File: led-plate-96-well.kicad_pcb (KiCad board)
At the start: 2 copper layers, 154.9 x 93.3 mm, 10 parts, among them J2 RAPC722X, U1 R-78E5.0-0.5, U2 A000053

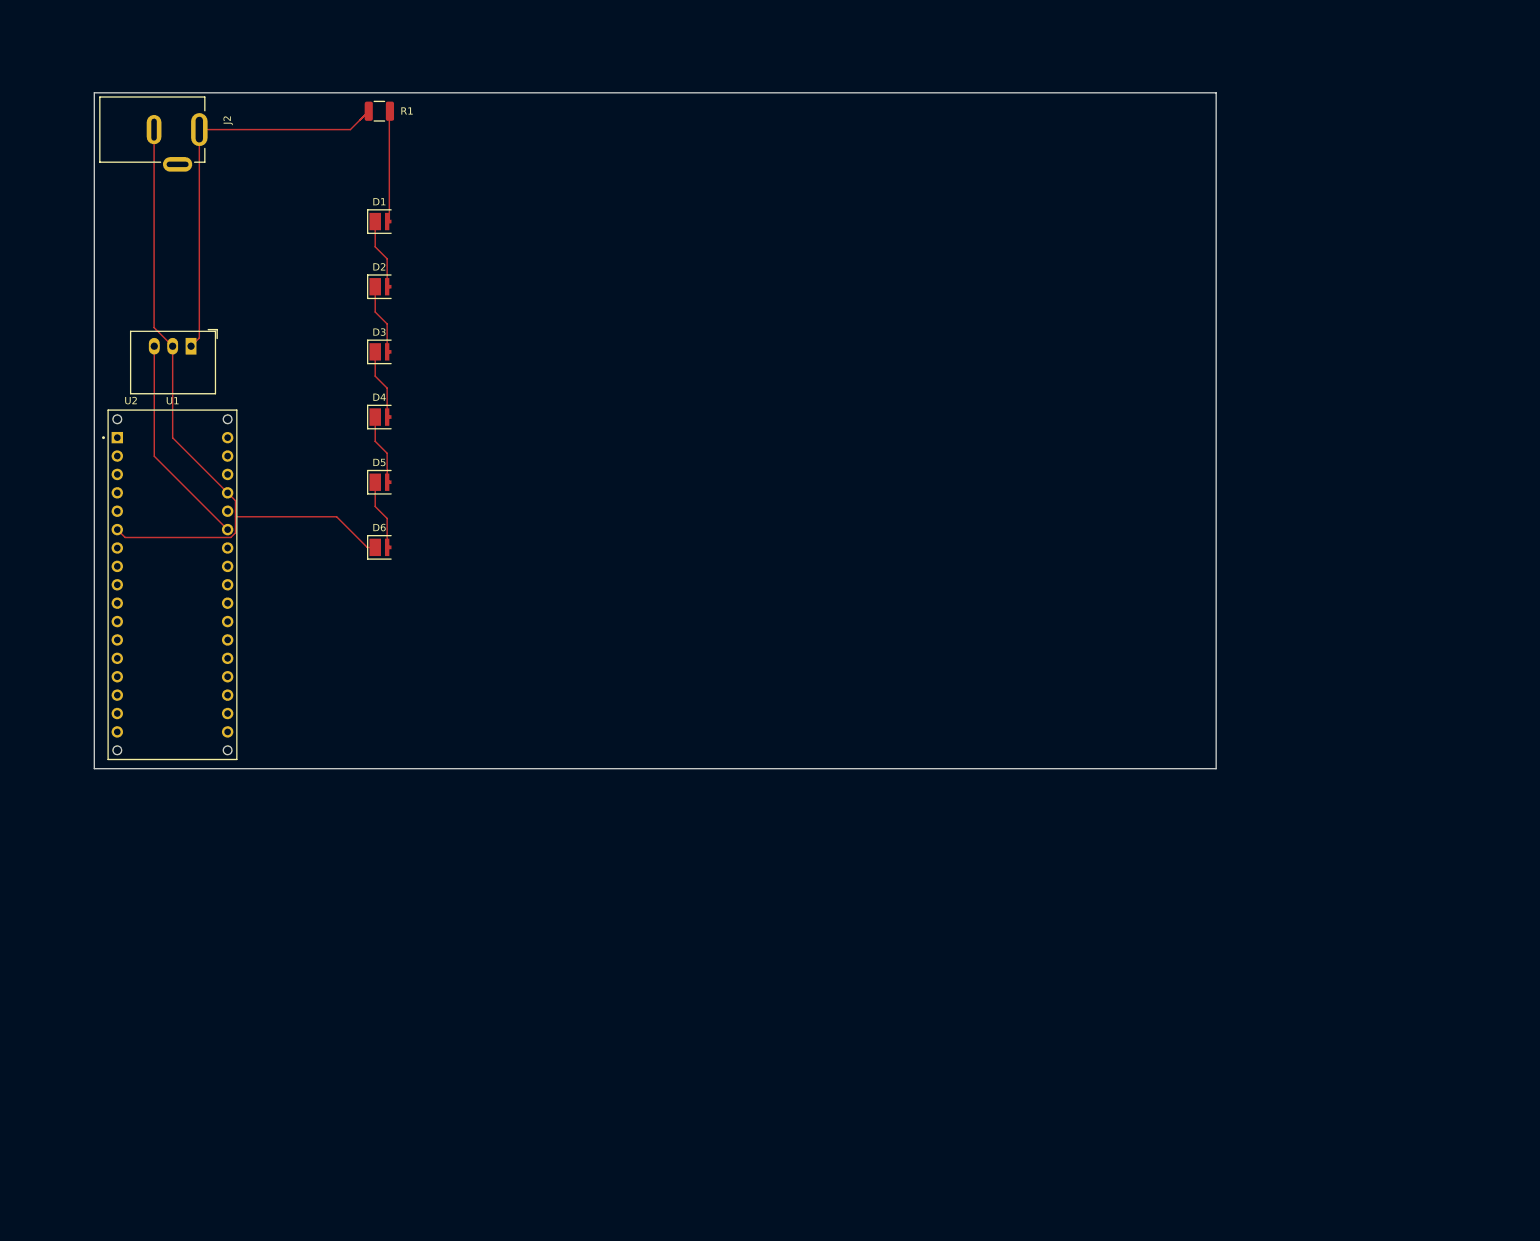
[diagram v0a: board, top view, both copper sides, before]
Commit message: basic led layout started
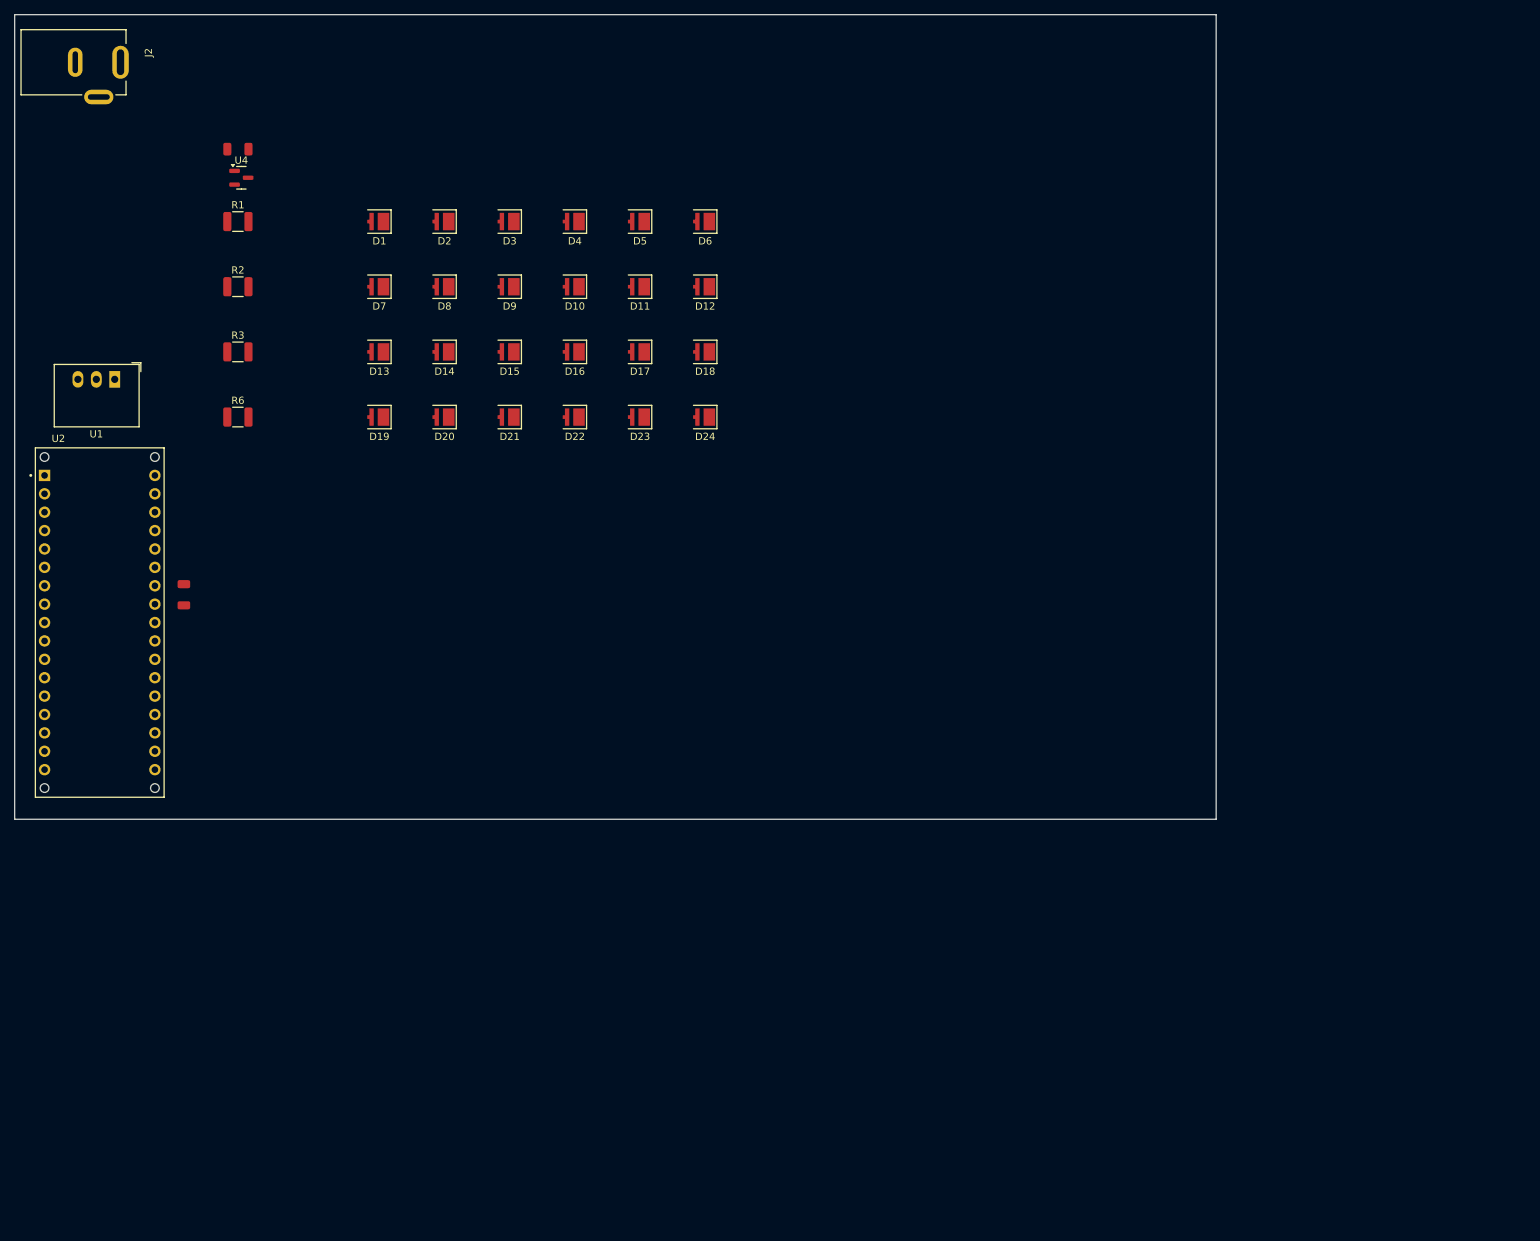
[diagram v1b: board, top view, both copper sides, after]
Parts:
- added D10: LED, LED_SMD:LED_Luminus_MP-3030-1100_3.0x3.0mm, F.Cu at (152.6, 51.2)
- added D11: LED, LED_SMD:LED_Luminus_MP-3030-1100_3.0x3.0mm, F.Cu at (161.6, 51.2)
- added D12: LED, LED_SMD:LED_Luminus_MP-3030-1100_3.0x3.0mm, F.Cu at (170.6, 51.2)
- added D13: LED, LED_SMD:LED_Luminus_MP-3030-1100_3.0x3.0mm, F.Cu at (125.6, 60.2)
- added D14: LED, LED_SMD:LED_Luminus_MP-3030-1100_3.0x3.0mm, F.Cu at (134.6, 60.2)
- added D15: LED, LED_SMD:LED_Luminus_MP-3030-1100_3.0x3.0mm, F.Cu at (143.6, 60.2)
- added D16: LED, LED_SMD:LED_Luminus_MP-3030-1100_3.0x3.0mm, F.Cu at (152.6, 60.2)
- added D17: LED, LED_SMD:LED_Luminus_MP-3030-1100_3.0x3.0mm, F.Cu at (161.6, 60.2)
- added D18: LED, LED_SMD:LED_Luminus_MP-3030-1100_3.0x3.0mm, F.Cu at (170.6, 60.2)
- added D19: LED, LED_SMD:LED_Luminus_MP-3030-1100_3.0x3.0mm, F.Cu at (125.6, 69.2)
- added D20: LED, LED_SMD:LED_Luminus_MP-3030-1100_3.0x3.0mm, F.Cu at (134.6, 69.2)
- added D21: LED, LED_SMD:LED_Luminus_MP-3030-1100_3.0x3.0mm, F.Cu at (143.6, 69.2)
- added D22: LED, LED_SMD:LED_Luminus_MP-3030-1100_3.0x3.0mm, F.Cu at (152.6, 69.2)
- added D23: LED, LED_SMD:LED_Luminus_MP-3030-1100_3.0x3.0mm, F.Cu at (161.6, 69.2)
- added D24: LED, LED_SMD:LED_Luminus_MP-3030-1100_3.0x3.0mm, F.Cu at (170.6, 69.2)
- added D7: LED, LED_SMD:LED_Luminus_MP-3030-1100_3.0x3.0mm, F.Cu at (125.6, 51.2)
- added D8: LED, LED_SMD:LED_Luminus_MP-3030-1100_3.0x3.0mm, F.Cu at (134.6, 51.2)
- added D9: LED, LED_SMD:LED_Luminus_MP-3030-1100_3.0x3.0mm, F.Cu at (143.6, 51.2)
- added R2: R, Resistor_SMD:R_1210_3225Metric, F.Cu at (106.0, 51.2)
- added R3: R, Resistor_SMD:R_1210_3225Metric, F.Cu at (106.0, 60.2)
- added R4: 100mΩ, PCM_JLCPCB:R_1206, F.Cu at (106.0, 32.2)
- added R5: 10kΩ, PCM_JLCPCB:R_1206, F.Cu at (98.6, 93.8)
- added R6: R, Resistor_SMD:R_1210_3225Metric, F.Cu at (106.0, 69.2)
- added U4: WST2N7002, Package_TO_SOT_SMD:SOT-23, F.Cu at (106.5, 36.2)
- moved D6 63.6 mm to (170.6, 42.2), turned to 180 degrees
- moved D5 50.9 mm to (161.6, 42.2), turned to 180 degrees
- moved D4 38.2 mm to (152.6, 42.2), turned to 180 degrees
- moved D3 25.5 mm to (143.6, 42.2), turned to 180 degrees
- moved R1 24.8 mm to (106.0, 42.2)
- moved J2 14.3 mm to (83.6, 20.2)
- moved D2 12.7 mm to (134.6, 42.2), turned to 180 degrees
- moved U1 11.5 mm to (89.0, 64.0)
- moved U2 11.3 mm to (87.0, 97.6)
- turned D1 to 180 degrees
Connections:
- R1 pad 1: +24V -> Net-(U4-D)
- U2 pad 8: unconnected-(U2-3(PWM)/SCL-Pad8) -> Net-(U2-3(PWM)/SCL)
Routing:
- net GND: track 98.4 -> 0.00 mm
- net +24V: track 56.6 -> 0.00 mm
- net Net-(U1-OUT): track 29.5 -> 0.00 mm
- net Net-(D1-A): track 15.6 -> 0.00 mm
- net Net-(D5-K): track 9.98 -> 0.00 mm
- net Net-(D4-K): track 9.98 -> 0.00 mm
- net Net-(D2-K): track 9.98 -> 0.00 mm
- net Net-(D1-K): track 9.98 -> 0.00 mm
- net Net-(D3-K): track 9.98 -> 0.00 mm
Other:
- board size 154.9 x 93.3 mm -> 165.9 x 111.1 mm

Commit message: all 96 leds laid out
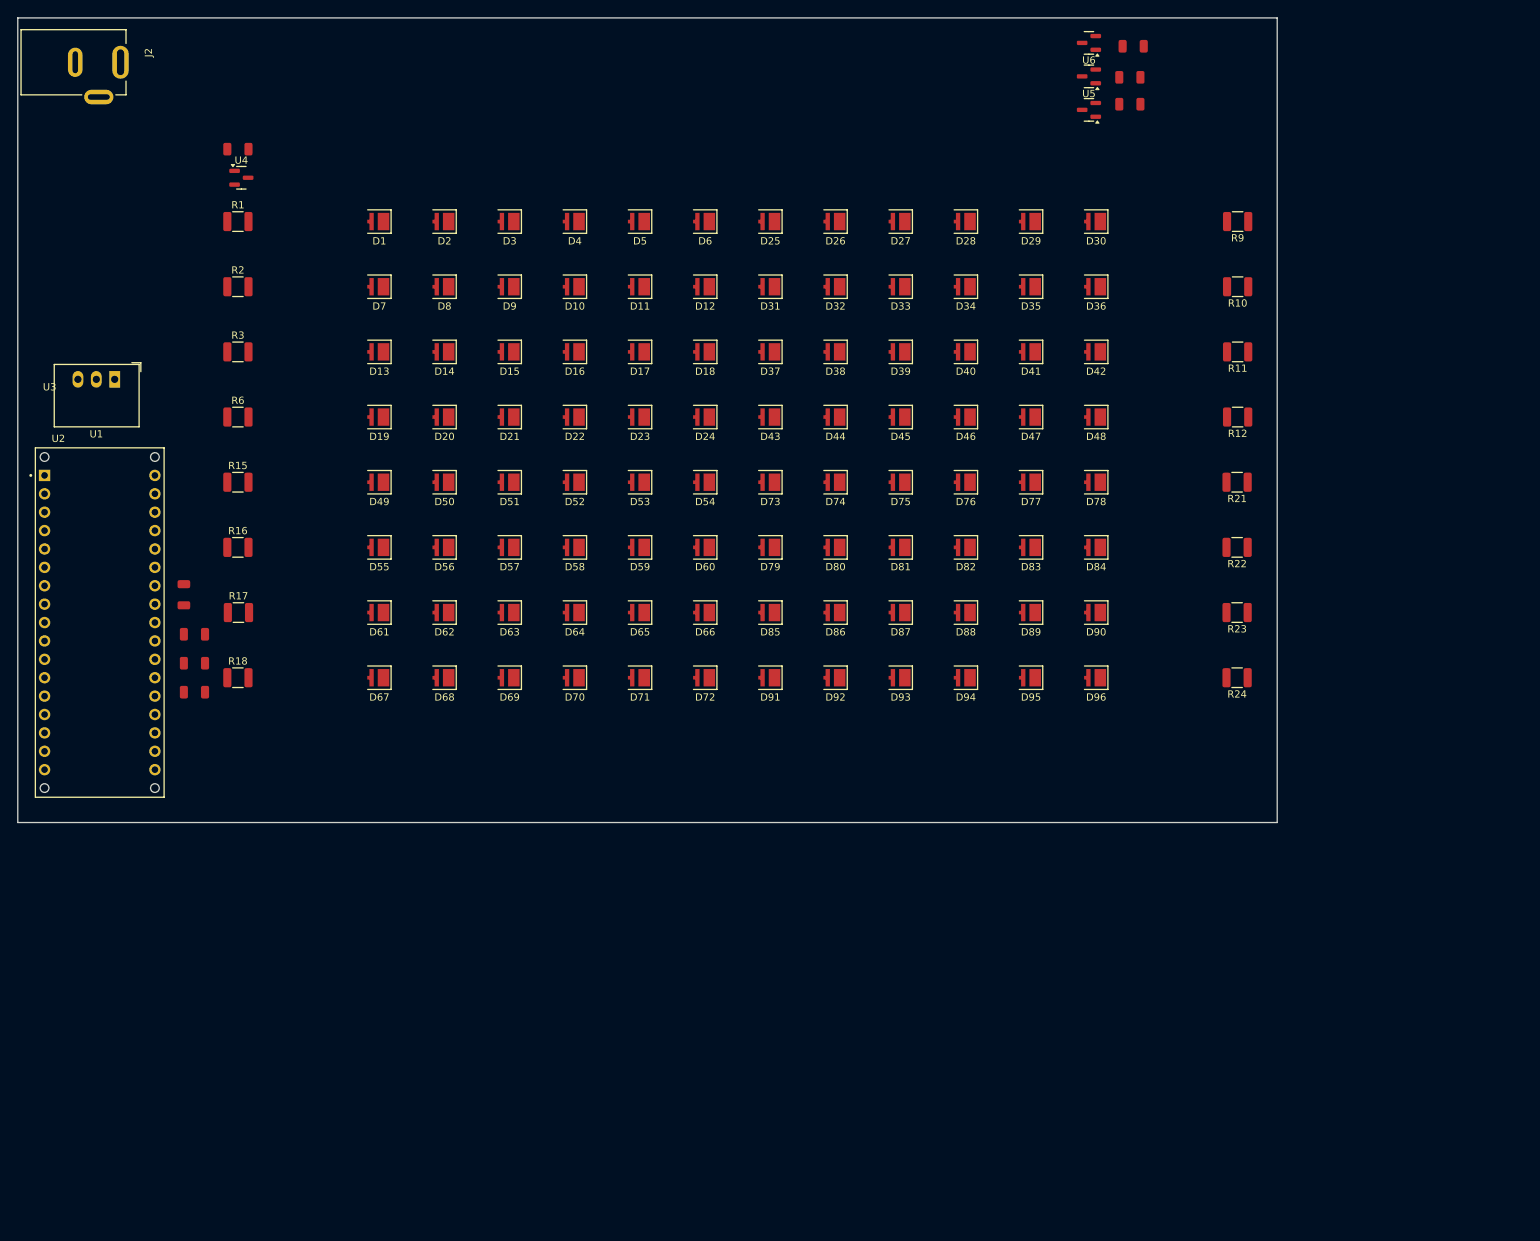
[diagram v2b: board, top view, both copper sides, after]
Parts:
- added D25: LED, LED_SMD:LED_Luminus_MP-3030-1100_3.0x3.0mm, F.Cu at (179.6, 42.2)
- added D26: LED, LED_SMD:LED_Luminus_MP-3030-1100_3.0x3.0mm, F.Cu at (188.6, 42.2)
- added D27: LED, LED_SMD:LED_Luminus_MP-3030-1100_3.0x3.0mm, F.Cu at (197.6, 42.2)
- added D28: LED, LED_SMD:LED_Luminus_MP-3030-1100_3.0x3.0mm, F.Cu at (206.6, 42.2)
- added D29: LED, LED_SMD:LED_Luminus_MP-3030-1100_3.0x3.0mm, F.Cu at (215.6, 42.2)
- added D30: LED, LED_SMD:LED_Luminus_MP-3030-1100_3.0x3.0mm, F.Cu at (224.6, 42.2)
- added D31: LED, LED_SMD:LED_Luminus_MP-3030-1100_3.0x3.0mm, F.Cu at (179.6, 51.2)
- added D32: LED, LED_SMD:LED_Luminus_MP-3030-1100_3.0x3.0mm, F.Cu at (188.6, 51.2)
- added D33: LED, LED_SMD:LED_Luminus_MP-3030-1100_3.0x3.0mm, F.Cu at (197.6, 51.2)
- added D34: LED, LED_SMD:LED_Luminus_MP-3030-1100_3.0x3.0mm, F.Cu at (206.6, 51.2)
- added D35: LED, LED_SMD:LED_Luminus_MP-3030-1100_3.0x3.0mm, F.Cu at (215.6, 51.2)
- added D36: LED, LED_SMD:LED_Luminus_MP-3030-1100_3.0x3.0mm, F.Cu at (224.6, 51.2)
- added D37: LED, LED_SMD:LED_Luminus_MP-3030-1100_3.0x3.0mm, F.Cu at (179.6, 60.2)
- added D38: LED, LED_SMD:LED_Luminus_MP-3030-1100_3.0x3.0mm, F.Cu at (188.6, 60.2)
- added D39: LED, LED_SMD:LED_Luminus_MP-3030-1100_3.0x3.0mm, F.Cu at (197.6, 60.2)
- added D40: LED, LED_SMD:LED_Luminus_MP-3030-1100_3.0x3.0mm, F.Cu at (206.6, 60.2)
- added D41: LED, LED_SMD:LED_Luminus_MP-3030-1100_3.0x3.0mm, F.Cu at (215.6, 60.2)
- added D42: LED, LED_SMD:LED_Luminus_MP-3030-1100_3.0x3.0mm, F.Cu at (224.6, 60.2)
- added D43: LED, LED_SMD:LED_Luminus_MP-3030-1100_3.0x3.0mm, F.Cu at (179.6, 69.2)
- added D44: LED, LED_SMD:LED_Luminus_MP-3030-1100_3.0x3.0mm, F.Cu at (188.6, 69.2)
- added D45: LED, LED_SMD:LED_Luminus_MP-3030-1100_3.0x3.0mm, F.Cu at (197.6, 69.2)
- added D46: LED, LED_SMD:LED_Luminus_MP-3030-1100_3.0x3.0mm, F.Cu at (206.6, 69.2)
- added D47: LED, LED_SMD:LED_Luminus_MP-3030-1100_3.0x3.0mm, F.Cu at (215.6, 69.2)
- added D48: LED, LED_SMD:LED_Luminus_MP-3030-1100_3.0x3.0mm, F.Cu at (224.6, 69.2)
- added D49: LED, LED_SMD:LED_Luminus_MP-3030-1100_3.0x3.0mm, F.Cu at (125.6, 78.2)
- added D50: LED, LED_SMD:LED_Luminus_MP-3030-1100_3.0x3.0mm, F.Cu at (134.6, 78.2)
- added D51: LED, LED_SMD:LED_Luminus_MP-3030-1100_3.0x3.0mm, F.Cu at (143.6, 78.2)
- added D52: LED, LED_SMD:LED_Luminus_MP-3030-1100_3.0x3.0mm, F.Cu at (152.6, 78.2)
- added D53: LED, LED_SMD:LED_Luminus_MP-3030-1100_3.0x3.0mm, F.Cu at (161.6, 78.2)
- added D54: LED, LED_SMD:LED_Luminus_MP-3030-1100_3.0x3.0mm, F.Cu at (170.6, 78.2)
- added D55: LED, LED_SMD:LED_Luminus_MP-3030-1100_3.0x3.0mm, F.Cu at (125.6, 87.2)
- added D56: LED, LED_SMD:LED_Luminus_MP-3030-1100_3.0x3.0mm, F.Cu at (134.6, 87.2)
- added D57: LED, LED_SMD:LED_Luminus_MP-3030-1100_3.0x3.0mm, F.Cu at (143.6, 87.2)
- added D58: LED, LED_SMD:LED_Luminus_MP-3030-1100_3.0x3.0mm, F.Cu at (152.6, 87.2)
- added D59: LED, LED_SMD:LED_Luminus_MP-3030-1100_3.0x3.0mm, F.Cu at (161.6, 87.2)
- added D60: LED, LED_SMD:LED_Luminus_MP-3030-1100_3.0x3.0mm, F.Cu at (170.6, 87.2)
- added D61: LED, LED_SMD:LED_Luminus_MP-3030-1100_3.0x3.0mm, F.Cu at (125.6, 96.2)
- added D62: LED, LED_SMD:LED_Luminus_MP-3030-1100_3.0x3.0mm, F.Cu at (134.6, 96.2)
- added D63: LED, LED_SMD:LED_Luminus_MP-3030-1100_3.0x3.0mm, F.Cu at (143.6, 96.2)
- added D64: LED, LED_SMD:LED_Luminus_MP-3030-1100_3.0x3.0mm, F.Cu at (152.6, 96.2)
- added D65: LED, LED_SMD:LED_Luminus_MP-3030-1100_3.0x3.0mm, F.Cu at (161.6, 96.2)
- added D66: LED, LED_SMD:LED_Luminus_MP-3030-1100_3.0x3.0mm, F.Cu at (170.6, 96.2)
- added D67: LED, LED_SMD:LED_Luminus_MP-3030-1100_3.0x3.0mm, F.Cu at (125.6, 105.2)
- added D68: LED, LED_SMD:LED_Luminus_MP-3030-1100_3.0x3.0mm, F.Cu at (134.6, 105.2)
- added D69: LED, LED_SMD:LED_Luminus_MP-3030-1100_3.0x3.0mm, F.Cu at (143.6, 105.2)
- added D70: LED, LED_SMD:LED_Luminus_MP-3030-1100_3.0x3.0mm, F.Cu at (152.6, 105.2)
- added D71: LED, LED_SMD:LED_Luminus_MP-3030-1100_3.0x3.0mm, F.Cu at (161.6, 105.2)
- added D72: LED, LED_SMD:LED_Luminus_MP-3030-1100_3.0x3.0mm, F.Cu at (170.6, 105.2)
- added D73: LED, LED_SMD:LED_Luminus_MP-3030-1100_3.0x3.0mm, F.Cu at (179.6, 78.2)
- added D74: LED, LED_SMD:LED_Luminus_MP-3030-1100_3.0x3.0mm, F.Cu at (188.6, 78.2)
- added D75: LED, LED_SMD:LED_Luminus_MP-3030-1100_3.0x3.0mm, F.Cu at (197.6, 78.2)
- added D76: LED, LED_SMD:LED_Luminus_MP-3030-1100_3.0x3.0mm, F.Cu at (206.6, 78.2)
- added D77: LED, LED_SMD:LED_Luminus_MP-3030-1100_3.0x3.0mm, F.Cu at (215.6, 78.2)
- added D78: LED, LED_SMD:LED_Luminus_MP-3030-1100_3.0x3.0mm, F.Cu at (224.6, 78.2)
- added D79: LED, LED_SMD:LED_Luminus_MP-3030-1100_3.0x3.0mm, F.Cu at (179.6, 87.2)
- added D80: LED, LED_SMD:LED_Luminus_MP-3030-1100_3.0x3.0mm, F.Cu at (188.6, 87.2)
- added D81: LED, LED_SMD:LED_Luminus_MP-3030-1100_3.0x3.0mm, F.Cu at (197.6, 87.2)
- added D82: LED, LED_SMD:LED_Luminus_MP-3030-1100_3.0x3.0mm, F.Cu at (206.6, 87.2)
- added D83: LED, LED_SMD:LED_Luminus_MP-3030-1100_3.0x3.0mm, F.Cu at (215.6, 87.2)
- added D84: LED, LED_SMD:LED_Luminus_MP-3030-1100_3.0x3.0mm, F.Cu at (224.6, 87.2)
- added D85: LED, LED_SMD:LED_Luminus_MP-3030-1100_3.0x3.0mm, F.Cu at (179.6, 96.2)
- added D86: LED, LED_SMD:LED_Luminus_MP-3030-1100_3.0x3.0mm, F.Cu at (188.6, 96.2)
- added D87: LED, LED_SMD:LED_Luminus_MP-3030-1100_3.0x3.0mm, F.Cu at (197.6, 96.2)
- added D88: LED, LED_SMD:LED_Luminus_MP-3030-1100_3.0x3.0mm, F.Cu at (206.6, 96.2)
- added D89: LED, LED_SMD:LED_Luminus_MP-3030-1100_3.0x3.0mm, F.Cu at (215.6, 96.2)
- added D90: LED, LED_SMD:LED_Luminus_MP-3030-1100_3.0x3.0mm, F.Cu at (224.6, 96.2)
- added D91: LED, LED_SMD:LED_Luminus_MP-3030-1100_3.0x3.0mm, F.Cu at (179.6, 105.2)
- added D92: LED, LED_SMD:LED_Luminus_MP-3030-1100_3.0x3.0mm, F.Cu at (188.6, 105.2)
- added D93: LED, LED_SMD:LED_Luminus_MP-3030-1100_3.0x3.0mm, F.Cu at (197.6, 105.2)
- added D94: LED, LED_SMD:LED_Luminus_MP-3030-1100_3.0x3.0mm, F.Cu at (206.6, 105.2)
- added D95: LED, LED_SMD:LED_Luminus_MP-3030-1100_3.0x3.0mm, F.Cu at (215.6, 105.2)
- added D96: LED, LED_SMD:LED_Luminus_MP-3030-1100_3.0x3.0mm, F.Cu at (224.6, 105.2)
- added R10: R, Resistor_SMD:R_1210_3225Metric, F.Cu at (244.1, 51.2)
- added R11: R, Resistor_SMD:R_1210_3225Metric, F.Cu at (244.1, 60.2)
- added R12: R, Resistor_SMD:R_1210_3225Metric, F.Cu at (244.1, 69.2)
- added R13: 10kΩ, PCM_JLCPCB:R_1206, F.Cu at (100.0, 103.2)
- added R14: 100mΩ, PCM_JLCPCB:R_1206, F.Cu at (229.2, 22.3)
- added R15: R, Resistor_SMD:R_1210_3225Metric, F.Cu at (106.0, 78.2)
- added R16: R, Resistor_SMD:R_1210_3225Metric, F.Cu at (106.0, 87.2)
- added R17: R, Resistor_SMD:R_1210_3225Metric, F.Cu at (106.1, 96.2)
- added R18: R, Resistor_SMD:R_1210_3225Metric, F.Cu at (106.0, 105.2)
- added R19: 10kΩ, PCM_JLCPCB:R_1206, F.Cu at (100.0, 99.2)
- added R20: 100mΩ, PCM_JLCPCB:R_1206, F.Cu at (229.7, 18.0)
- added R21: R, Resistor_SMD:R_1210_3225Metric, F.Cu at (244.0, 78.2)
- added R22: R, Resistor_SMD:R_1210_3225Metric, F.Cu at (244.0, 87.2)
- added R23: R, Resistor_SMD:R_1210_3225Metric, F.Cu at (244.0, 96.2)
- added R24: R, Resistor_SMD:R_1210_3225Metric, F.Cu at (244.0, 105.2)
- added R7: 10kΩ, PCM_JLCPCB:R_1206, F.Cu at (100.0, 107.2)
- added R8: 100mΩ, PCM_JLCPCB:R_1206, F.Cu at (229.2, 26.0)
- added R9: R, Resistor_SMD:R_1210_3225Metric, F.Cu at (244.1, 42.2)
- added U3: WST2N7002, Package_TO_SOT_SMD:SOT-23, F.Cu at (223.6, 26.8)
- added U5: WST2N7002, Package_TO_SOT_SMD:SOT-23, F.Cu at (223.6, 22.2)
- added U6: WST2N7002, Package_TO_SOT_SMD:SOT-23, F.Cu at (223.6, 17.5)
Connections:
- U2 pad 10: unconnected-(U2-5(PWM)-Pad10) -> Net-(U2-5(PWM))
- U2 pad 11: unconnected-(U2-6(PWM)/A7-Pad11) -> Net-(U2-6(PWM)/A7)
- U2 pad 14: unconnected-(U2-9(PWM)/A9-Pad14) -> Net-(U2-9(PWM)/A9)
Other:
- board size 165.9 x 111.1 mm -> 173.9 x 111.1 mm

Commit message: basic pcb layout done
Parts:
- moved R7 164.7 mm to (244.0, 27.2), turned to 0 degrees
- moved R14 154.8 mm to (106.1, 116.2), turned to 0 degrees
- moved U5 147.2 mm to (105.6, 110.3), turned to 90 degrees
- moved R19 138.5 mm to (237.1, 119.2)
- moved R20 99.3 mm to (244.1, 116.2), turned to 0 degrees
- moved U6 96.0 mm to (244.5, 111.2), turned to -90 degrees
- moved R5 59.1 mm to (101.6, 34.8), turned to -90 degrees
- moved J2 32.0 mm to (84.6, 52.2)
- moved U3 23.0 mm to (244.5, 36.2), turned to -90 degrees
- moved R13 17.1 mm to (106.0, 119.2), turned to 0 degrees
- moved R8 15.8 mm to (244.1, 31.2), turned to 0 degrees
- moved R4 1.00 mm to (106.1, 31.2)
- moved U4 0.13 mm to (106.6, 36.3), turned to -90 degrees
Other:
- board size 173.9 x 111.1 mm -> 172.9 x 99.1 mm

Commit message: auto route done
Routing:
- net GND: track 0.00 -> 466.8 mm, vias 0 -> 9
- net Net-(U2-5(PWM)): track 0.00 -> 236.6 mm, vias 0 -> 1
- net Net-(U2-6(PWM)/A7): track 0.00 -> 172.6 mm
- net Net-(U2-3(PWM)/SCL): track 0.00 -> 87.2 mm, vias 0 -> 1
- net Net-(D31-A): track 0.00 -> 67.2 mm
- net Net-(D43-A): track 0.00 -> 66.6 mm
- net Net-(D37-A): track 0.00 -> 66.6 mm
- net Net-(D25-A): track 0.00 -> 66.6 mm
- net Net-(D91-A): track 0.00 -> 66.5 mm
- net Net-(D79-A): track 0.00 -> 66.5 mm
- net Net-(D73-A): track 0.00 -> 66.5 mm
- net Net-(D85-A): track 0.00 -> 66.2 mm
- net Net-(U6-D): track 0.00 -> 34.3 mm
- net Net-(U4-D): track 0.00 -> 32.8 mm
- net Net-(U3-D): track 0.00 -> 32.5 mm
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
